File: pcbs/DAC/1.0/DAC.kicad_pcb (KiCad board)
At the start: 2 copper layers, 85 x 55 mm, 67 parts, among them J1 Conn_01x03_Pin, J11 Conn_01x03_Pin, J2 Conn_01x03_Pin, J3 Conn_01x03_Pin, J4 Conn_01x02_Pin, J5 Conn_01x03_Pin, J6 Conn_01x02_Pin, J7 Conn_01x04_Pin, J8 Conn_01x04_Pin, J9 Conn_01x04_Pin, U1 DA101C_C6931652, U2 AMS1117-3.3, U3 PCM5122PW, U4 PCM5122PW, U5 PCM5122PW

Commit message: Updates
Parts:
- moved C34 0.76 mm to (103.9, 95.9)
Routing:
- net LEFT_TWEETER: track 11.4 -> 12.1 mm
- net AGND: vias 9 -> 8

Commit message: Updating PCBs
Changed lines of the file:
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@@
+	)
+	(segment
+		(start 143.0364 72.665)
+		(end 139.9364 69.565)
+		(width 0.25)
+		(layer "F.Cu")
+		(net 6)
 	)
 	(segment
@@
 	)
 	(segment
+		(start 139.9364 69.565)
+		(end 139.9364 69.165)
+		(width 0.25)
+		(layer "F.Cu")
+		(net 6)
+	)
+	(segment
 		(start 113.161399 91.4275)
 		(end 110.6739 91.4275)
@@
 	)
 	(segment
-		(start 142.6364 93.265)
-		(end 142.4364 93.465)
-		(width 0.25)
-		(layer "F.Cu")
-		(net 6)
-	)
-	(segment
-		(start 141.9364 94.665)
-		(end 140.4364 94.665)
-		(width 0.25)
-		(layer "F.Cu")
-		(net 6)
-	)
-	(segment
 		(start 113.4864 92.49)
 		(end 113.4864 91.752501)
@@
 	)
 	(segment
-		(start 142.4364 94.165)
-		(end 141.9364 94.665)
-		(width 0.25)
-		(layer "F.Cu")
-		(net 6)
-	)
-	(segment
-		(start 105.4989 95.935)
-		(end 105.6864 95.7475)
-		(width 0.25)
-		(layer "F.Cu")
-		(net 6)
-	)
-	(segment
 		(start 113.5739 92.5775)
 		(end 113.4864 92.49)
@@
 	)
 	(segment
-		(start 142.6364 71.865)
-		(end 142.6364 93.265)
-		(width 0.25)
-		(layer "F.Cu")
-		(net 6)
-	)
-	(segment
 		(start 89.8864 91.752501)
 		(end 90.211401 91.4275)
@@
 	)
 	(segment
+		(start 143.0364 92.965)
+		(end 143.0364 72.665)
+		(width 0.25)
+		(layer "F.Cu")
+		(net 6)
+	)
+	(segment
 		(start 105.6864 91.752501)
 		(end 106.011401 91.4275)
@@
 	)
 	(segment
+		(start 141.3364 94.665)
+		(end 143.0364 92.965)
+		(width 0.25)
+		(layer "F.Cu")
+		(net 6)
+	)
+	(segment
 		(start 85.3614 95.935)
 		(end 85.9864 95.31)
@@
 	)
 	(segment
-		(start 139.9364 69.165)
-		(end 142.6364 71.865)
+		(start 140.4364 94.665)
+		(end 141.3364 94.665)
 		(width 0.25)
 		(layer "F.Cu")
@@
 	)
 	(segment
-		(start 142.4364 93.465)
-		(end 142.4364 94.165)
-		(width 0.25)
-		(layer "F.Cu")
-		(net 6)
-	)
-	(segment
 		(start 139.2364 95.865)
 		(end 140.4364 94.665)
@@
 	)
 	(segment
-		(start 141.0614 77.79)
-		(end 141.0614 90.04)
+		(start 141.5364 78.265)
+		(end 139.9364 76.665)
 		(width 0.25)
 		(layer "F.Cu")
@@
 	)
 	(segment
-		(start 141.0614 90.04)
-		(end 140.4364 90.665)
-		(width 0.25)
-		(layer "F.Cu")
-		(net 7)
-	)
-	(segment
 		(start 131.3614 95.865)
 		(end 131.3614 94.19)
@@
 	)
 	(segment
-		(start 139.9364 76.665)
-		(end 141.0614 77.79)
+		(start 140.4364 90.665)
+		(end 141.5364 89.565)
 		(width 0.25)
 		(layer "F.Cu")
@@
 	)
 	(segment
+		(start 141.5364 89.565)
+		(end 141.5364 78.265)
+		(width 0.25)
+		(layer "F.Cu")
+		(net 7)
+	)
+	(segment
 		(start 131.3614 94.19)
 		(end 133.2364 92.315)
@@
 	)
 	(segment
+		(start 111.7364 88.765)
+		(end 114.644458 91.673058)
+		(width 0.25)
+		(layer "F.Cu")
+		(net 11)
+	)
+	(segment
 		(start 64.9864 88.015)
 		(end 65.5364 88.565)
@@
 	)
 	(segment
-		(start 106.0364 89.265)
-		(end 112.2364 89.265)
-		(width 0.25)
-		(layer "F.Cu")
-		(net 11)
-	)
-	(segment
-		(start 112.2364 89.265)
-		(end 114.7364 91.765)
-		(width 0.25)
-		(layer "F.Cu")
-		(net 11)
-	)
-	(segment
 		(start 105.723899 88.765)
 		(end 105.5364 88.765)
@@
 	)
 	(segment
+		(start 105.5364 88.765)
+		(end 111.7364 88.765)
+		(width 0.25)
+		(layer "F.Cu")
+		(net 11)
+	)
+	(segment
 		(start 85.9864 86.765)
 		(end 85.9864 87.632635)
@@
 	)
 	(segment
-		(start 105.5364 88.765)
-		(end 106.0364 89.265)
-		(width 0.25)
-		(layer "F.Cu")
-		(net 11)
-	)
-	(segment
 		(start 84.0364 88.865)
 		(end 83.9364 88.965)
@@
 	)
 	(segment
+		(start 114.644458 91.673058)
+		(end 114.828342 91.673058)
+		(width 0.25)
+		(layer "F.Cu")
+		(net 11)
+	)
+	(segment
 		(start 72.4364 90.265)
 		(end 72.8364 89.865)
@@
 	)
 	(via
-		(at 114.7364 91.765)
+		(at 114.828342 91.673058)
 		(size 0.5)
 		(drill 0.3)
@@
 	)
 	(segment
-		(start 114.7364 91.765)
-		(end 114.972796 91.765)
+		(start 124.1364 104.065)
+		(end 124.1364 100.828604)
 		(width 0.25)
 		(layer "B.Cu")
@@
 	)
 	(segment
-		(start 124.1364 100.928604)
-		(end 124.1364 104.065)
+		(start 114.980854 91.673058)
+		(end 114.828342 91.673058)
+		(width 0.25)
+		(layer "B.Cu")
+		(net 11)
+	)
+	(segment
+		(start 124.1364 100.828604)
+		(end 114.980854 91.673058)
 		(width 0.25)
 		(layer "B.Cu")
@@
 	)
 	(segment
-		(start 114.972796 91.765)
-		(end 124.1364 100.928604)
-		(width 0.25)
-		(layer "B.Cu")
-		(net 11)
-	)
-	(segment
 		(start 106.3364 87.502499)
 		(end 105.744722 88.094177)
@@
 	(segment
 		(start 117.7364 96.865)
-		(end 115.5364 94.665)
+		(end 117.7364 95.465)
+		(width 0.25)
+		(layer "B.Cu")
+		(net 12)
+	)
+	(segment
+		(start 117.7364 95.465)
+		(end 110.365577 88.094177)
 		(width 0.25)
 		(layer "B.Cu")
@@
 	)
 	(segment
-		(start 115.5364 94.665)
-		(end 115.5364 93.365)
-		(width 0.25)
-		(layer "B.Cu")
-		(net 12)
-	)
-	(segment
 		(start 84.9364 88.265)
 		(end 72.7114 88.265)
@@
 	)
 	(segment
+		(start 110.365577 88.094177)
+		(end 105.200989 88.094177)
+		(width 0.25)
+		(layer "B.Cu")
+		(net 12)
+	)
+	(segment
 		(start 94.0364 88.165)
 		(end 105.130166 88.165)
@@
 	)
 	(segment
-		(start 112.7364 93.365)
-		(end 107.465577 88.094177)
-		(width 0.25)
-		(layer "B.Cu")
-		(net 12)
-	)
-	(segment
-		(start 107.465577 88.094177)
-		(end 105.200989 88.094177)
-		(width 0.25)
-		(layer "B.Cu")
-		(net 12)
-	)
-	(segment
-		(start 115.5364 93.365)
-		(end 112.7364 93.365)
-		(width 0.25)
-		(layer "B.Cu")
-		(net 12)
-	)
-	(segment
 		(start 108.2864 95.898666)
 		(end 107.2364 96.948666)
@@
 	)
 	(segment
-		(start 110.2364 94.359699)
+		(start 110.2364 94.665199)
 		(end 110.2364 101.865)
 		(width 0.4)
@@
 	)
 	(segment
+		(start 109.5864 94.015199)
+		(end 110.2364 94.665199)
+		(width 0.4)
+		(layer "F.Cu")
+		(net 26)
+	)
+	(segment
 		(start 109.5864 92.49)
-		(end 109.5864 93.709699)
-		(width 0.4)
-		(layer "F.Cu")
-		(net 26)
-	)
-	(segment
-		(start 109.5864 93.709699)
-		(end 110.2364 94.359699)
+		(end 109.5864 94.015199)
 		(width 0.4)
 		(layer "F.Cu")
@@
 	)
 	(segment
-		(start 110.8614 94.136171)
-		(end 110.8614 94.441671)
+		(start 110.2364 93.816671)
+		(end 111.6364 95.216671)
 		(width 0.4)
 		(layer "F.Cu")
@@
 	)
 	(segment
-		(start 110.2364 93.511171)
-		(end 110.8614 94.136171)
+		(start 111.6364 108.59)
+		(end 111.0614 109.165)
 		(width 0.4)
 		(layer "F.Cu")
@@
 	(segment
 		(start 110.2364 92.49)
-		(end 110.2364 93.511171)
-		(width 0.4)
-		(layer "F.Cu")
-		(net 28)
-	)
-	(segment
-		(start 110.8614 94.441671)
-		(end 111.6364 95.216671)
-		(width 0.4)
-		(layer "F.Cu")
-		(net 28)
-	)
-	(segment
-		(start 111.6364 108.59)
-		(end 111.0614 109.165)
+		(end 110.2364 93.816671)
 		(width 0.4)
 		(layer "F.Cu")
@@
 	)
 	(segment
+		(start 108.4364 82.258834)
+		(end 108.4364 75.565)
+		(width 0.4)
+		(layer "F.Cu")
+		(net 44)
+	)
+	(segment
 		(start 109.5864 83.408834)
 		(end 108.4364 82.258834)
@@
 	)
 	(segment
-		(start 108.4364 74.665)
+		(start 107.7364 74.865)
 		(end 107.7364 73.965)
 		(width 0.4)
@@
 	)
 	(segment
-		(start 108.4364 82.258834)
-		(end 108.4364 74.665)
+		(start 108.4364 75.565)
+		(end 107.7364 74.865)
 		(width 0.4)
 		(layer "F.Cu")
@@
 		(polygon
 			(pts
-				(xy 56.7364 88.765) (xy 124.8364 88.765) (xy 124.8364 73.665) (xy 124.3364 73.165) (xy 135.2364 73.165)
-				(xy 135.8364 73.765) (xy 135.8364 57.465) (xy 135.7364 57.365) (xy 144.7364 57.365) (xy 145.2364 57.865)
-				(xy 145.2364 114.965) (xy 59.1364 114.965) (xy 53.1364 108.965) (xy 53.1364 92.365)
+				(xy 56.7364 88.765) (xy 124.9364 88.765) (xy 124.9364 73.765) (xy 125.0364 73.865) (xy 135.8364 73.765)
+				(xy 135.8364 57.465) (xy 135.7364 57.365) (xy 144.7364 57.365) (xy 145.2364 57.865) (xy 145.2364 114.965)
+				(xy 59.1364 114.965) (xy 53.1364 108.965) (xy 53.1364 92.365)
 			)
 		)
@@
 		(polygon
 			(pts
-				(xy 135.7364 57.365) (xy 135.7364 73.165) (xy 135.2364 73.665) (xy 124.8364 73.665) (xy 124.8364 88.765)
+				(xy 135.7364 57.365) (xy 135.7364 73.165) (xy 135.2364 73.665) (xy 124.6364 73.665) (xy 124.6364 88.765)
 				(xy 56.7364 88.765) (xy 56.7364 56.565) (xy 57.2364 56.065) (xy 134.4364 56.065)
 			)

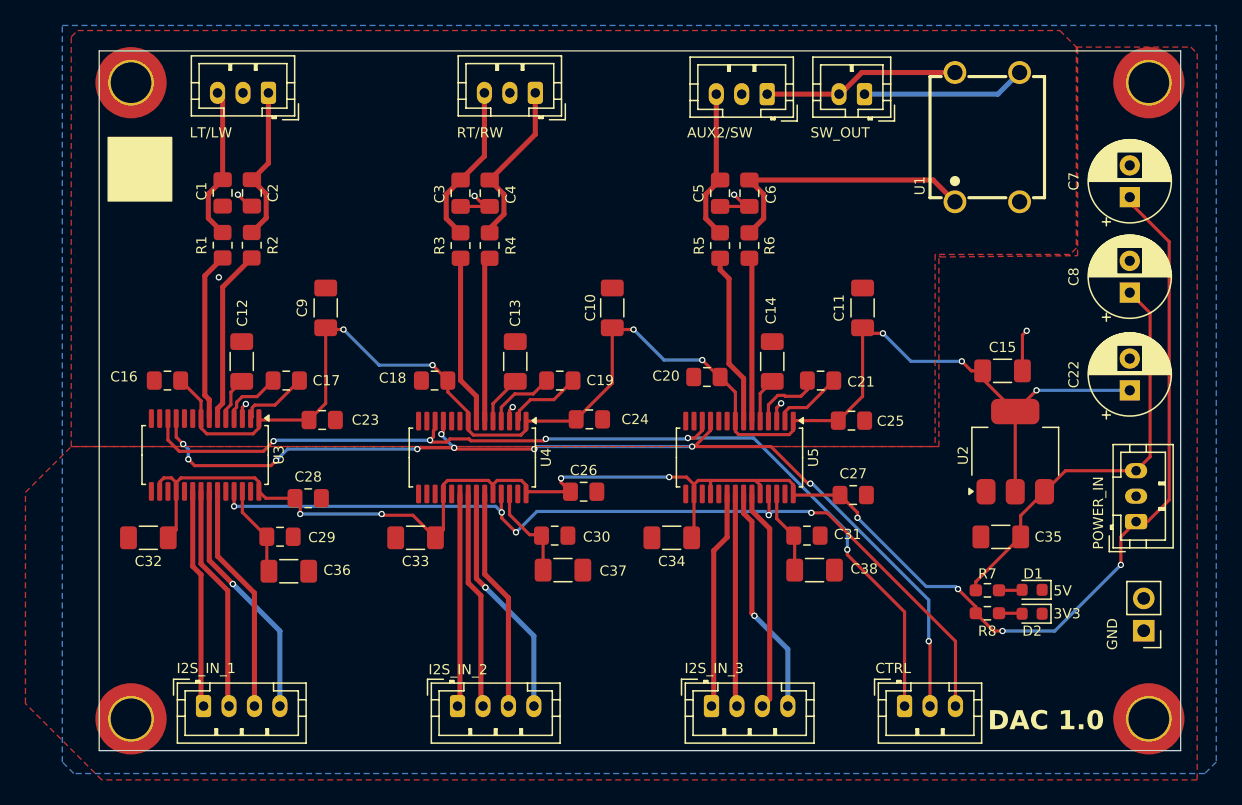
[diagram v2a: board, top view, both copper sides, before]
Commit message: Updated screenshots
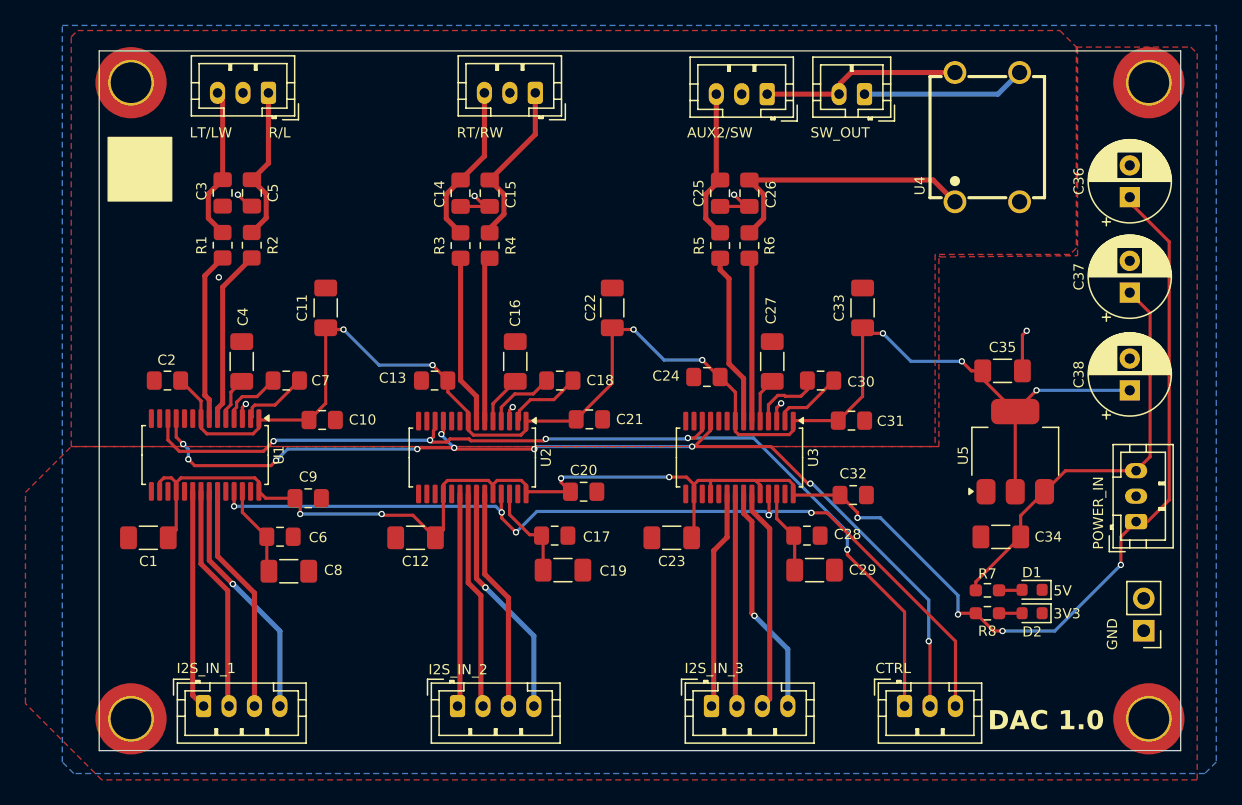
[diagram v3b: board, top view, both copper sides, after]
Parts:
- renumbered C32 to C1, C23 to C10, C9 to C11, C33 to C12, C18 to C13, C3 to C14, C4 to C15, C13 to C16, C30 to C17, C19 to C18, C37 to C19, C16 to C2, C26 to C20, C24 to C21, C10 to C22, C34 to C23, C20 to C24, C5 to C25, C6 to C26, C14 to C27, C31 to C28, C38 to C29, C1 to C3, C21 to C30, C25 to C31, C27 to C32, C11 to C33, C35 to C34, C15 to C35, C7 to C36, C8 to C37, C22 to C38, C12 to C4, C2 to C5, C29 to C6, C17 to C7, C36 to C8, C28 to C9, H3 to H2, H2 to H3, J7 to J1, J6 to J10, J1 to J2, J8 to J3, J2 to J4, J9 to J5, J3 to J6, J4 to J7, J11 to J8, J5 to J9, U3 to U1, U4 to U2, U5 to U3, U1 to U4, U2 to U5
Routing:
- net 3V3: track 139.3 -> 139.9 mm
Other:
- board text added: "R/L"
